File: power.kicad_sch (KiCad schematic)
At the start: 12 parts, among them IC1 MP9943AGQ-Z, IC2 MP9943AGQ-Z, U4 AP2112K-3.3TRG1, U5 AP2112K-1.8TRG1

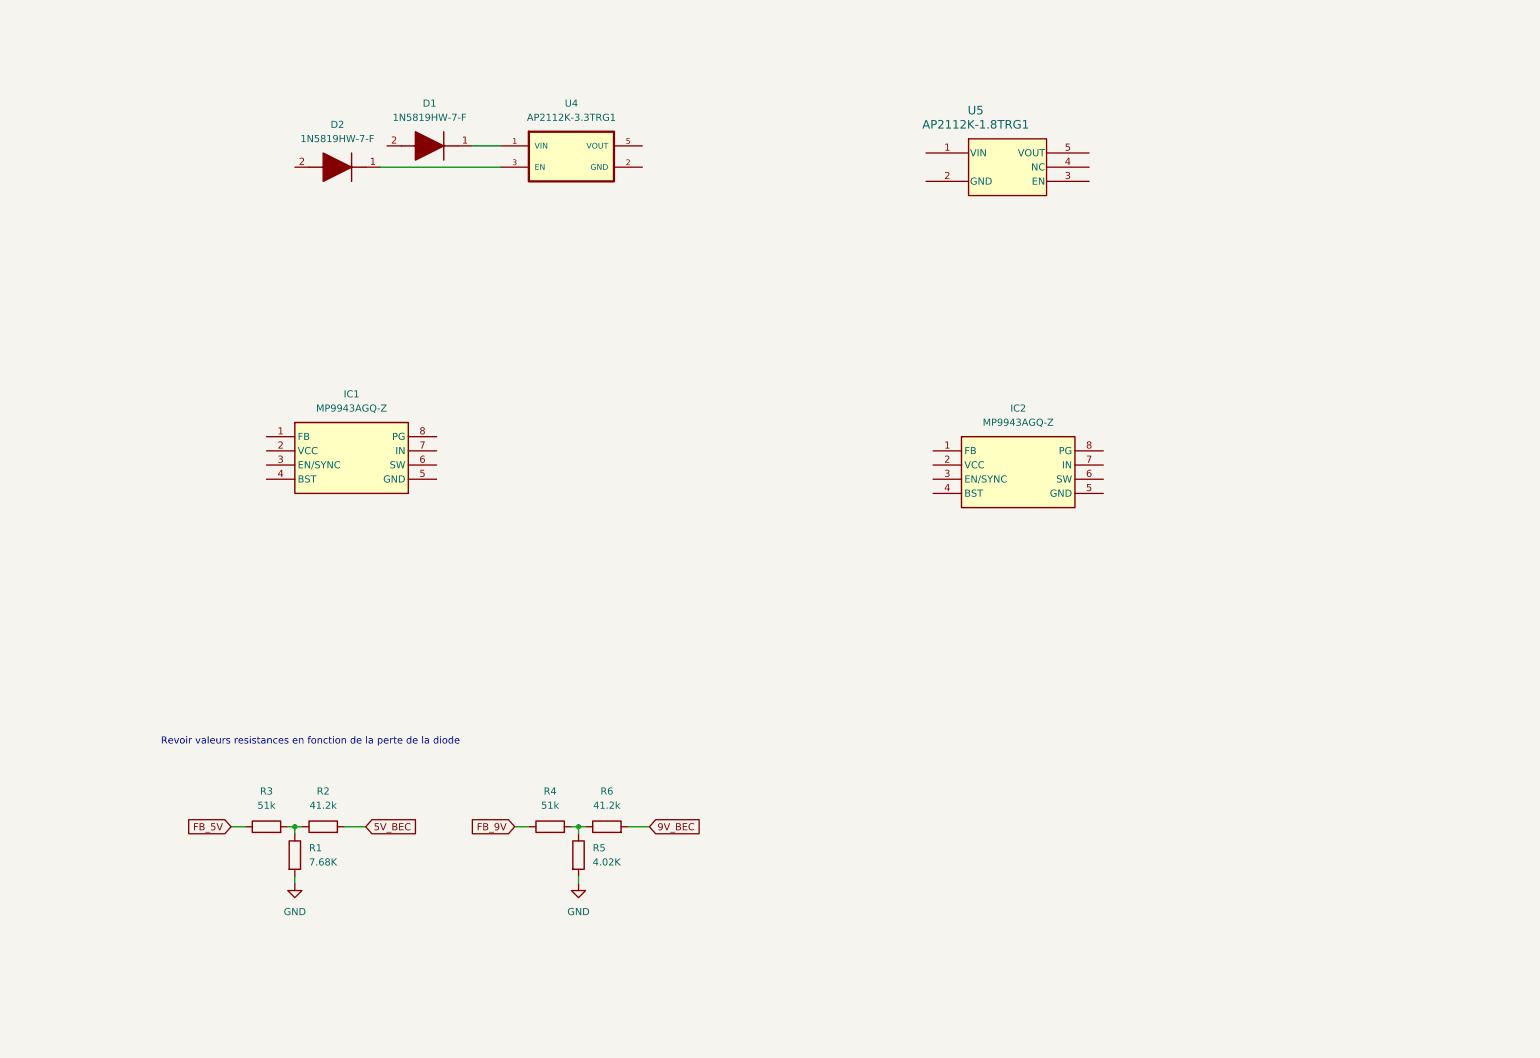
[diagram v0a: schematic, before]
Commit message: first components on schematic and few wiring
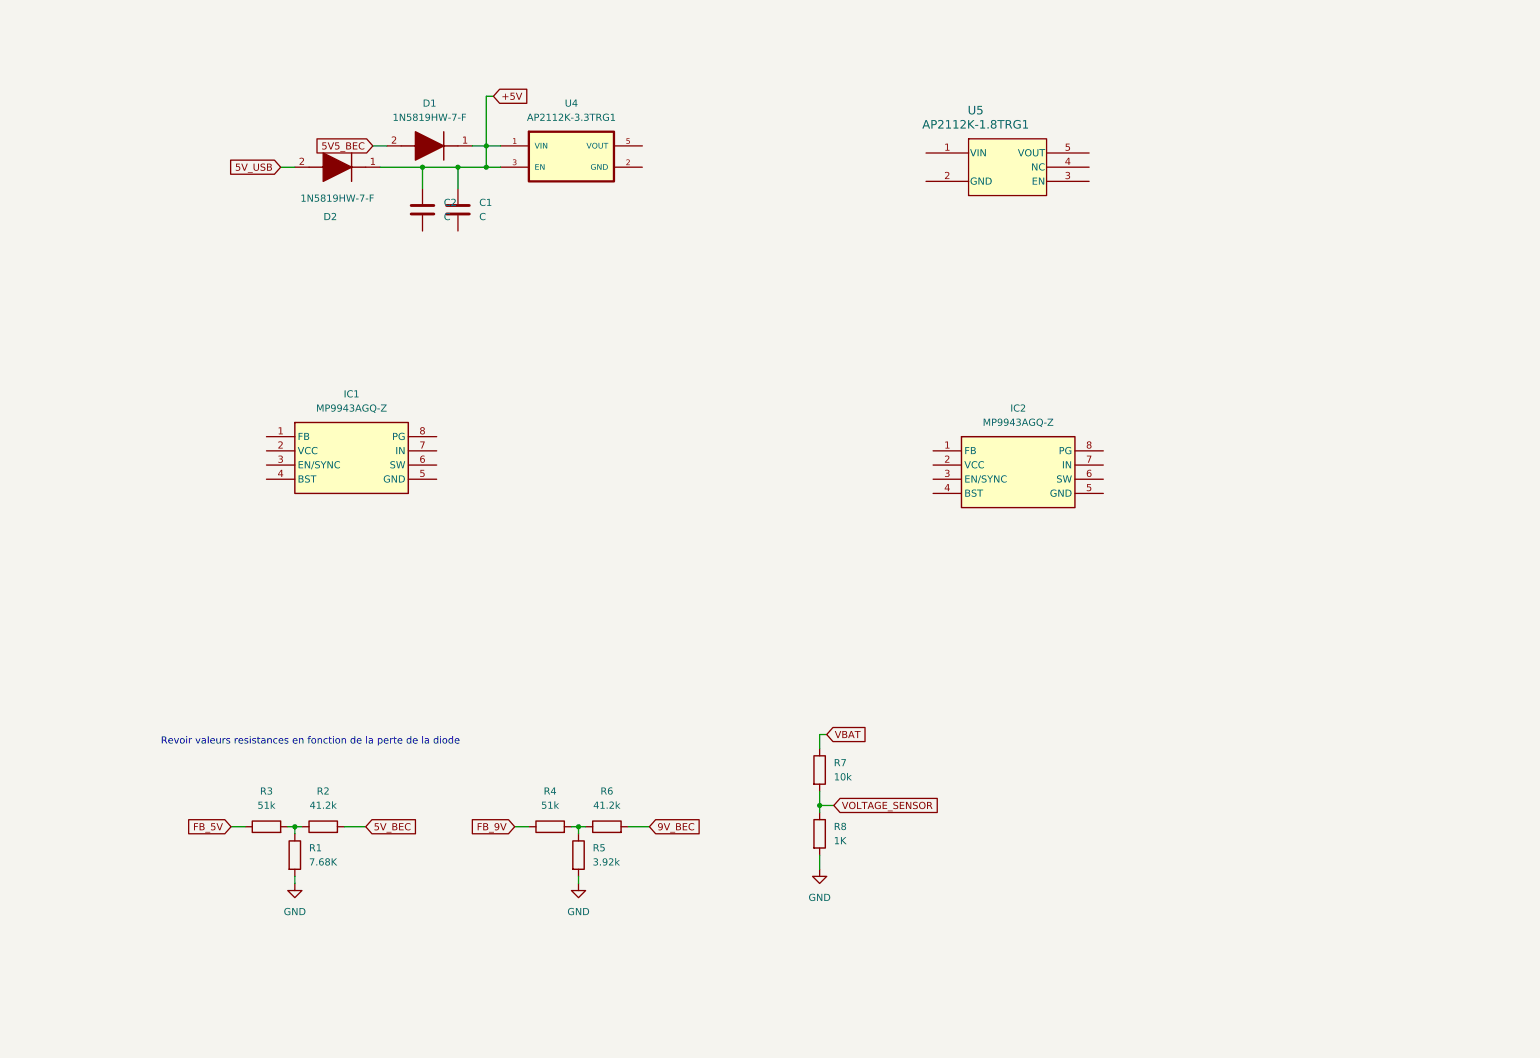
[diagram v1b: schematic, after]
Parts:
- added C1, C2: C, symbol Device:C
- added R7: 10k, symbol Device:R
- added R8: 1K, symbol Device:R
- R5: value 4.02K -> 3.92k
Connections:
- net GND: now also R8.2
- net +5V: now reaches D1.1 (K), U4.1 (VIN)
- net +5V: now also D2.1 (K), U4.3 (EN), C1.1, C2.1
- net 5V5_BEC: now reaches D1.2 (A)
- net 5V_USB: now reaches D2.2 (A)
- new net VBAT: R7.1
- new net VOLTAGE_SENSOR: R7.2, R8.1

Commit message: Refactor sensor.kicad_sch: Adjust component positions and update property attributes for ICM-42688-P
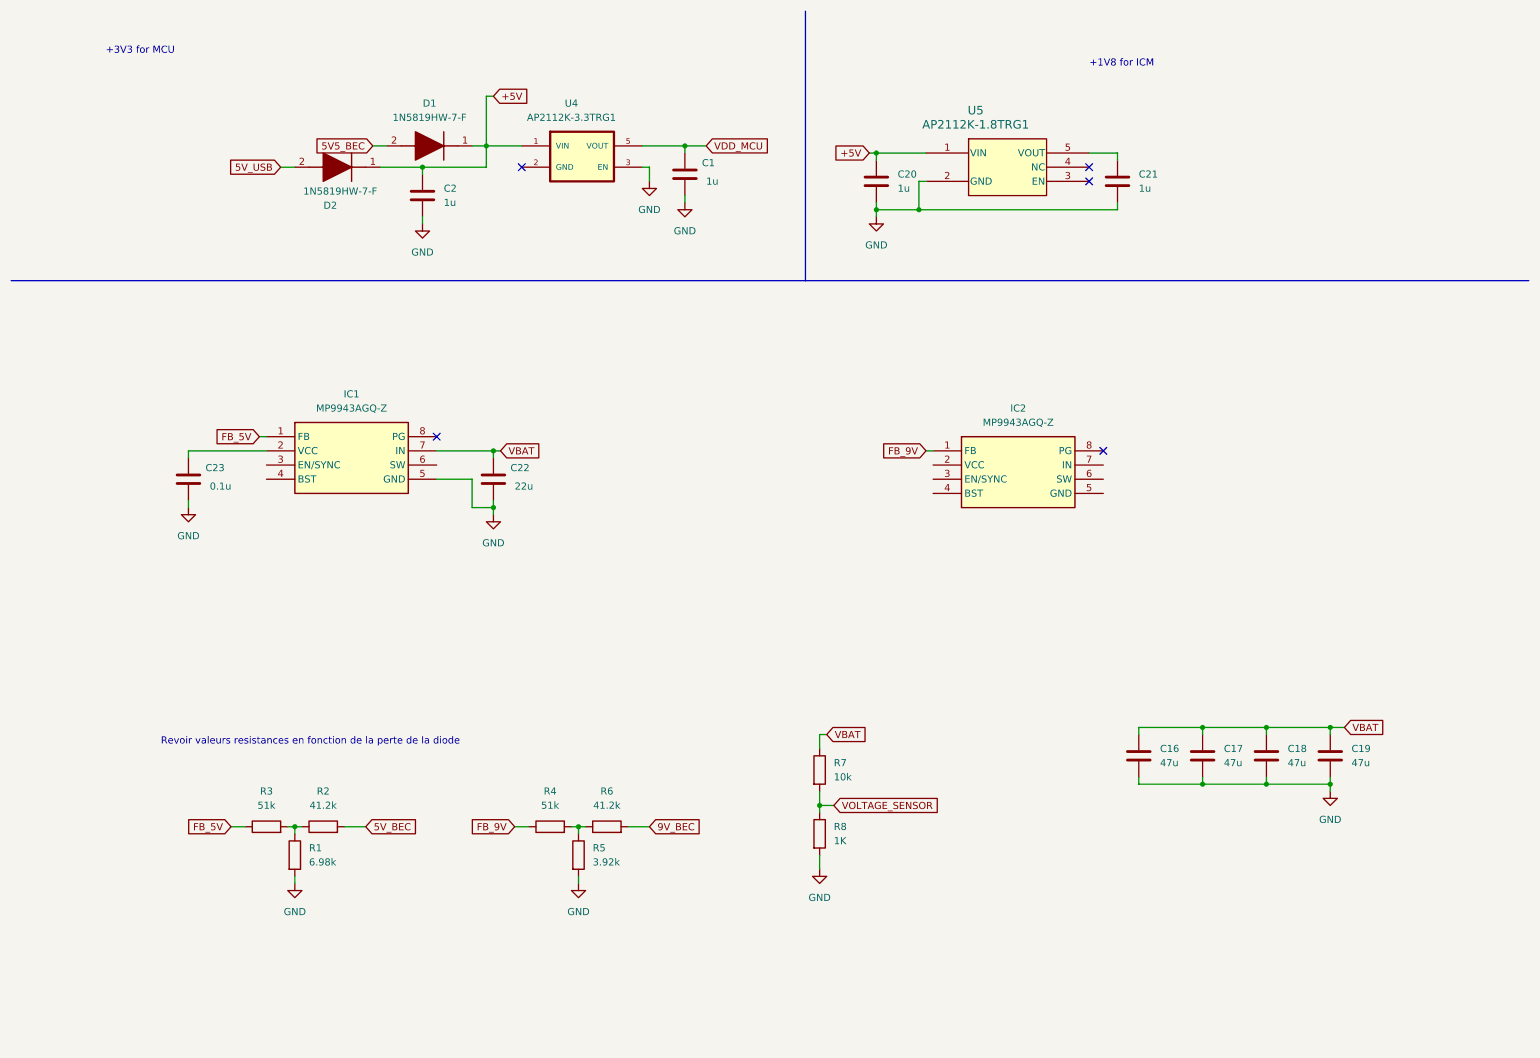
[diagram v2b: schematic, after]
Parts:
- added C16, C17, C18, C19: 47u, symbol Device:C
- added C20, C21: 1u, symbol Device:C
- added C22: 22u, symbol Device:C
- added C23: 0.1u, symbol Device:C
- C1, C2: value C -> 1u
- R1: value 7.68K -> 6.98k
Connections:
- net +5V: now also U5.1 (VIN), C20.1; no longer C1.1, U4.3 (EN)
- net FB_5V: now also IC1.1 (FB)
- net FB_9V: now also IC2.1 (FB)
- net GND: now also C1.2, C2.2, IC1.5 (GND), U4.3 (EN), U5.2 (GND), C16.2, C17.2, C18.2, C19.2, C20.2, C21.2, C22.2, C23.2
- net VBAT: now also IC1.7 (IN), C16.1, C17.1, C18.1, C19.1, C22.1
- net at U5.5 (VOUT): now also C21.1
- net VDD_MCU: now reaches U4.5 (VOUT)
- net VDD_MCU: now also C1.1
- net at IC1.2 (VCC): now also C23.1
- no-connect marks 0 -> 5
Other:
- note added: "+1V8 for ICM"
- note added: "+3V3 for MCU"
- moved on the sheet: C2, U4

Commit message: finished buck schematic and designed solder pads footprints
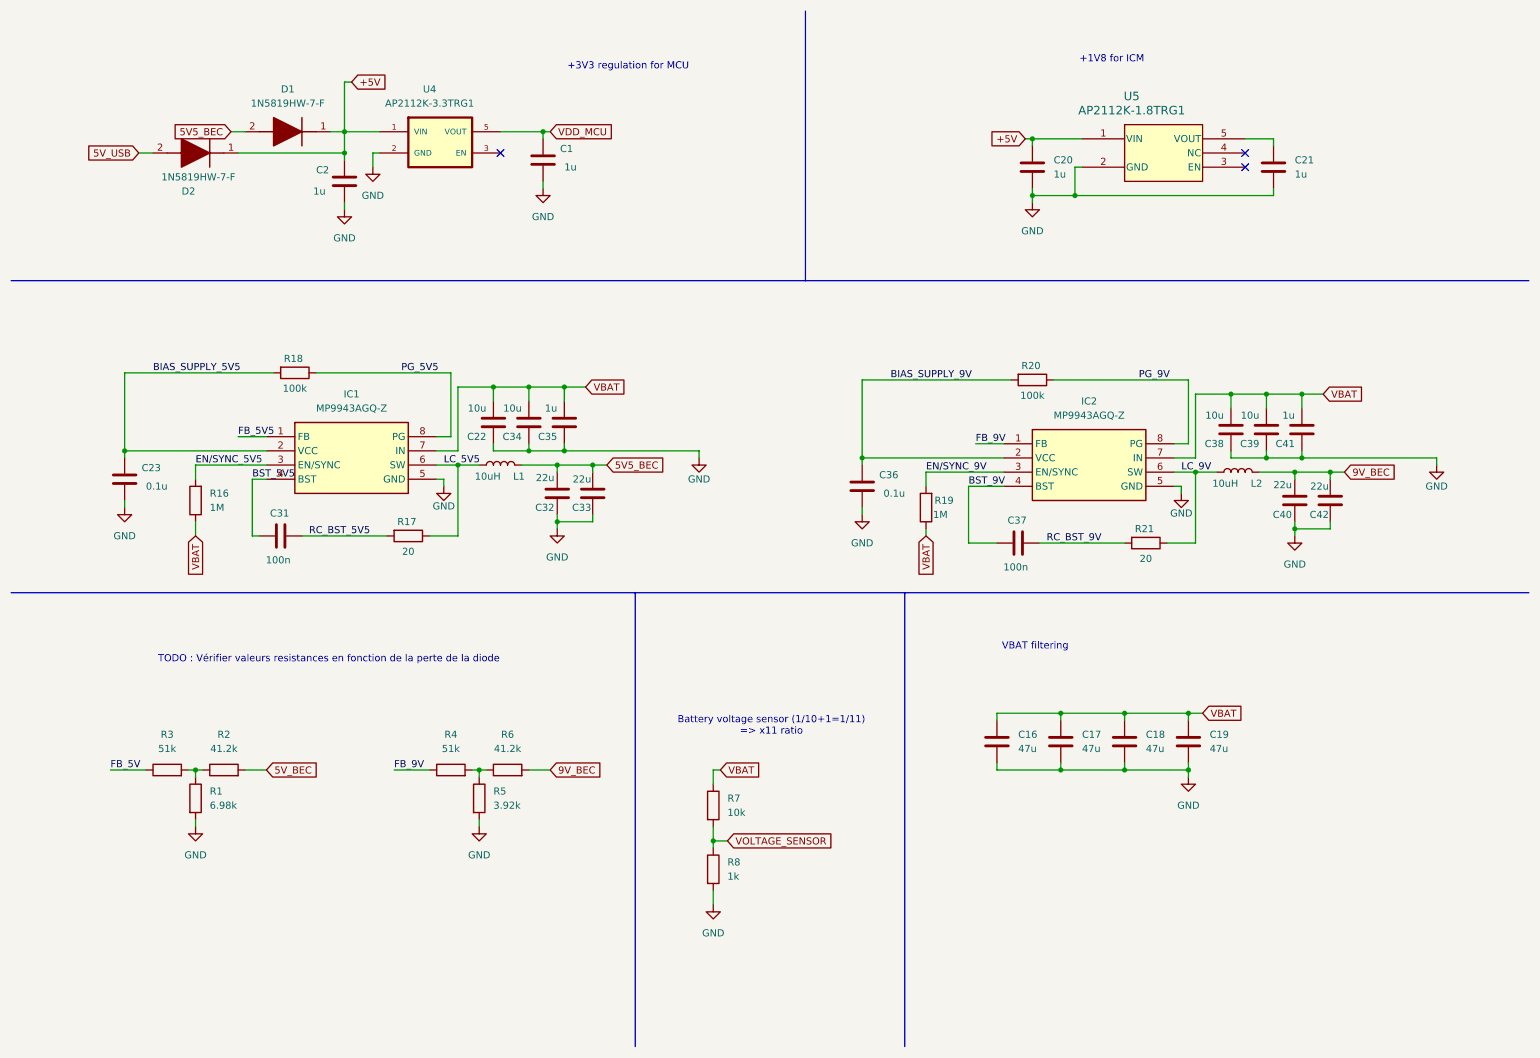
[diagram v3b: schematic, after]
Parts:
- added C31, C37: 100n, symbol Device:C
- added C32, C33, C40, C42: 22u, symbol Device:C
- added C34, C38, C39: 10u, symbol Device:C
- added C35, C41: 1u, symbol Device:C
- added C36: 0.1u, symbol Device:C
- added L1, L2: 10uH, symbol Device:L
- added R16, R19: 1M, symbol Device:R
- added R17, R21: 20, symbol Device:R
- added R18, R20: 100k, symbol Device:R
- C22: value 22u -> 10u
- R8: value 1K -> 1k
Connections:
- net 5V5_BEC: now also C32.2, C33.2, L1.2
- net 9V_BEC: now also C40.2, C42.2, L2.2
- net FB_5V: no longer IC1.1 (FB)
- net GND: now also C22.1, IC2.5 (GND), U4.2 (GND), C32.1, C33.1, C34.1, C35.1, C36.2, C38.1, C39.1, C40.1, C41.1, C42.1; no longer C22.2, U4.3 (EN)
- net VBAT: now also C22.2, IC2.7 (IN), C34.2, C35.2, C38.2, C39.2, C41.2, R16.1, R19.1; no longer C22.1
- net BIAS_SUPPLY_5V5: now reaches C23.1, IC1.2 (VCC)
- net BIAS_SUPPLY_5V5: now also R18.2
- net BIAS_SUPPLY_9V: now reaches IC2.2 (VCC)
- net BIAS_SUPPLY_9V: now also C36.1, R20.2
- net EN/SYNC_9V: now reaches IC2.3 (EN/SYNC)
- net EN/SYNC_9V: now also R19.2
- net BST_9V: now reaches IC2.4 (BST)
- net BST_9V: now also C37.1
- net LC_9V: now reaches IC2.6 (SW)
- net LC_9V: now also L2.1, R21.1
- net PG_9V: now reaches IC2.8 (PG)
- net PG_9V: now also R20.1
- net EN/SYNC_5V5: now reaches IC1.3 (EN/SYNC)
- net EN/SYNC_5V5: now also R16.2
- net BST_5V5: now reaches IC1.4 (BST)
- net BST_5V5: now also C31.1
- net LC_5V5: now reaches IC1.6 (SW)
- net LC_5V5: now also L1.1, R17.1
- net PG_5V5: now reaches IC1.8 (PG)
- net PG_5V5: now also R18.1
- new net FB_5V5: IC1.1 (FB)
- new net RC_BST_5V5: C31.2, R17.2
- new net RC_BST_9V: C37.2, R21.2
- no-connect marks 5 -> 3
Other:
- note added: "+3V3 regulation for MCU"
- note added: "Battery voltage sensor (1/10+1=1/11) => x11 ratio"
- note added: "TODO : Vérifier valeurs resistances en fonction de la perte de la diode"
- note added: "VBAT filtering"
- note removed: "+3V3 for MCU"
- note removed: "Revoir valeurs resistances en fonction de la perte de la diode"
- moved on the sheet: C1, C16, C17, C18, C19, C2, C20, C21, C22, C23, D1, D2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

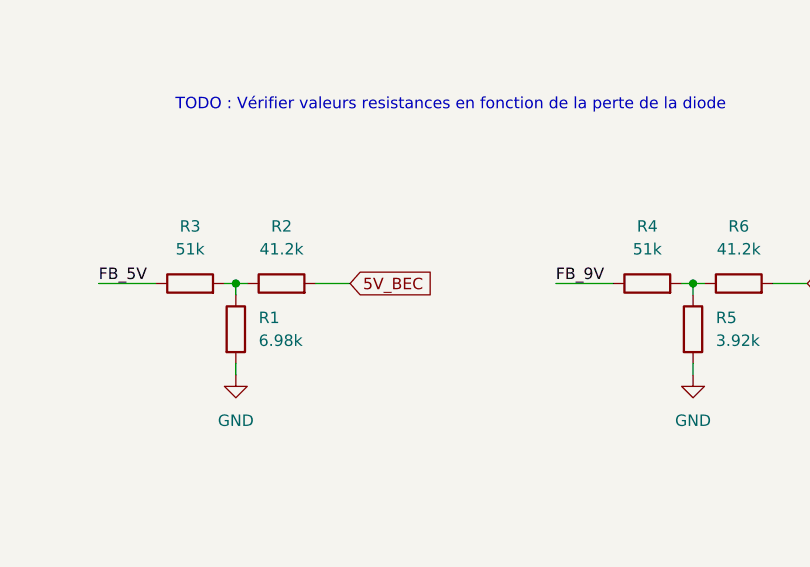
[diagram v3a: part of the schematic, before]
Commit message: add wiring to soldering pads for uart, dji, and esc
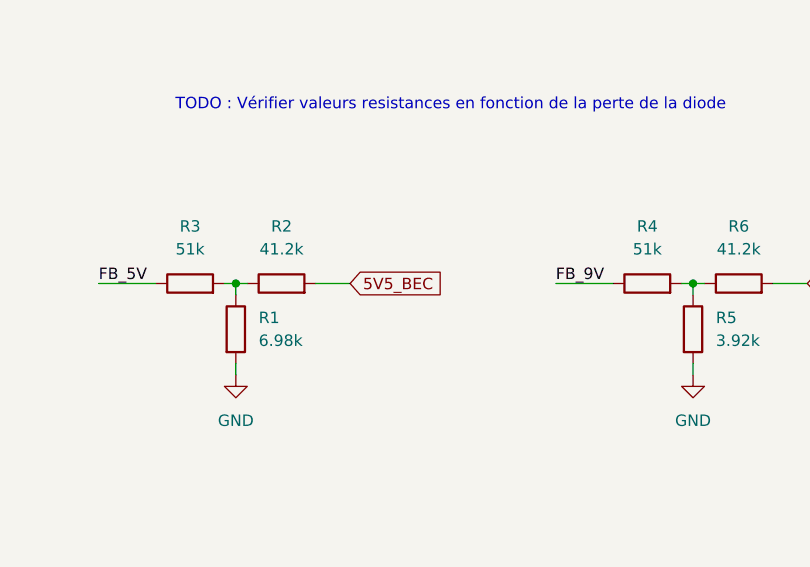
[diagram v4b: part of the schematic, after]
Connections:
- net 5V_BEC is gone; now on net 5V5_BEC: R2.2
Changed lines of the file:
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@@
 		)
 	)
-	(global_label "5V_BEC"
+	(global_label "5V5_BEC"
 		(shape input)
 		(at 58.42 148.59 0)
@@
 		)
 		(property "Intersheetrefs" "${INTERSHEET_REFS}"
-			(at 68.3599 148.59 0)
+			(at 69.5694 148.59 0)
 			(effects
 				(font
